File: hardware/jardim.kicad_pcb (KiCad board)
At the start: 2 copper layers, 100 x 100 mm, 67 parts, among them J1 DC_INPUT, J10 DHT22_AMB, J11 LIGHT_SENSOR_1, J12 LIGHT_SENSOR_2, J13 LEVEL_SENSOR_1, J14 LEVEL_SENSOR_2, J15 SOIL_HUMIDITY_SENSOR_1, J16 SOIL_HUMIDITY_SENSOR_2, J2 PUMP_1, J3 PUMP_2, J4 LIGHT_1, J5 LIGHT_2, J6 HEAT_2, J7 HEAT_2, J8 DS12B20_2, J9 DS18B20_1, Q1 IRLB8721, Q2 IRLB8721, Q3 IRLB8721, Q4 IRLB8721, Q5 IRLB8721, Q6 IRLB8721, U1 AM2302

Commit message: kicad otr
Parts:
- C1: value 100uF -> 220uF
- C5, C6, D3, Q2, R5, R6: moved to F.Cu
- R19, U1: moved to B.Cu
- moved J1 157.7 mm to (55.9, 45.8), turned to -90 degrees
- moved J2 121.7 mm to (55.9, 68.6), turned to -90 degrees
- moved J9 106.2 mm to (147.3, 83.7)
- moved J8 106.1 mm to (147.3, 71.1)
- moved J10 51.8 mm to (147.3, 96.4)
- moved J12 49.1 mm to (146.8, 125.7)
- moved J13 46.3 mm to (147.3, 134.6)
- moved J11 35.5 mm to (147.3, 111.7)
- moved J3 34.8 mm to (55.9, 81.3)
- moved J4 24.6 mm to (55.9, 94.0)
- moved J5 24.6 mm to (55.9, 106.7)
- moved J7 24.6 mm to (55.9, 132.1)
- moved J6 24.6 mm to (55.9, 119.4)
- moved R6 22.4 mm to (146.9, 45.7), turned to 180 degrees
- moved D3 20.8 mm to (125.3, 45.7)
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
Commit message: miniaturizando com grade menor
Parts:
- added SW1: SW_Push, Button_Switch_THT:SW_PUSH_6mm, F.Cu at (183.4, 118.4)
- added SW2: SW_Push, Button_Switch_THT:SW_PUSH_6mm, F.Cu at (183.4, 126.0)
- added SW3: SW_Push, Button_Switch_THT:SW_PUSH_6mm, F.Cu at (183.4, 133.6)
- added U2: DM-OLED096-636, oled:MODULE_DM-OLED096-636, F.Cu at (130.2, 125.1)
- R19, U1: moved to F.Cu
- moved R19 112.1 mm to (171.4, 65.4), turned to 180 degrees
- moved U1 82.8 mm to (148.0, 66.7), turned to 0 degrees
- moved J13 65.4 mm to (189.2, 84.4)
- moved J14 59.2 mm to (179.7, 84.6)
- moved R15 55.8 mm to (141.6, 99.1)
- moved J10 46.9 mm to (189.2, 75.5)
- moved D9 45.5 mm to (113.7, 127.6)
- moved D8 45.2 mm to (113.7, 116.2)
- moved D7 45.0 mm to (113.7, 104.8)
- moved D6 44.8 mm to (113.7, 93.3)
- moved R10 44.6 mm to (108.6, 109.9)
- moved R13 44.6 mm to (108.6, 112.4)
- moved R16 44.6 mm to (108.6, 125.1)
- moved R3 44.6 mm to (108.6, 71.8)
- moved R4 44.6 mm to (108.6, 84.5)
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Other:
- board text added: "220uF"
- board text added: "DC-DC 12V"
- board text added: "DC_IN_24V"
- board text added: "DHT22"
- board text added: "DOWN"
- board text added: "HEAT_1"
- board text added: "HEAT_2"
- board text added: "LIGHT_1"
- board text added: "LIGHT_2"
- board text added: "OK"
- board text added: "OLED 1306"
- board text added: "TEXTO"
- board text added: "UP"
- board text removed: "100uF"
- board text removed: "DC IN 24V"

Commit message: buzzer e textos
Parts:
- added BZ1: Buzzer, Buzzer_Beeper:Buzzer_12x9.5RM7.6, B.Cu at (161.9, 123.8)
- added D5: 1N5822, Diode_THT:D_DO-201AD_P15.24mm_Horizontal, B.Cu at (166.4, 133.3)
- added Q7: FQP30N06L, Package_TO_SOT_THT:TO-220-3_Horizontal_TabDown, B.Cu at (161.3, 105.1)
- added R20: 220, Resistor_THT:R_Axial_DIN0207_L6.3mm_D2.5mm_P10.16mm_Horizontal, B.Cu at (163.2, 111.1)
- added R21: 10k, Resistor_THT:R_Axial_DIN0207_L6.3mm_D2.5mm_P10.16mm_Horizontal, B.Cu at (163.2, 115.6)
- added SW4: SW_SPST, TerminalBlock_Phoenix:TerminalBlock_Phoenix_MKDS-1,5-2-5.08_1x02_P5.08mm_Horizontal, B.Cu at (100.8, 59.1)
- J6: value HEAT_2 -> HEAT_1
- Q1, Q2, Q3, Q4, Q5, Q6: value IRLB8721 -> FQP30N06L
- R19: footprint Resistor_THT:R_Axial_DIN0207_L6.3mm_D2.5mm_P10.16mm_Horizontal -> Resistor_THT:R_Axial_DIN0207_L6.3mm_D2.5mm_P7.62mm_Horizontal
- moved C1 68.1 mm to (163.8, 69.2)
- moved C2 67.5 mm to (168.9, 68.0)
- moved R13 7.75 mm to (114.9, 116.8)
- moved R3 7.75 mm to (114.9, 76.2)
- moved R4 7.75 mm to (114.9, 88.9)
- moved R10 7.75 mm to (114.9, 114.3)
- moved R16 7.75 mm to (114.9, 129.5)
- moved R7 7.75 mm to (114.9, 101.6)
- moved D4 5.85 mm to (109.9, 77.5)
- moved D7 5.85 mm to (109.9, 100.3)
- moved D9 5.85 mm to (109.9, 123.2)
- moved D2 5.85 mm to (109.9, 66.0)
- moved D6 5.85 mm to (109.9, 88.9)
- moved D8 5.85 mm to (109.9, 111.8)
- moved J2 3.17 mm to (100.8, 63.5)
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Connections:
- F1 pad 1: +24V -> Net-(SW4-B)
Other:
- board text added: "HEATER_1"
- board text added: "HEATER_2"
- board text added: "LEVEL_1"
- board text added: "LEVEL_2"
- board text added: "PUMP_1"
- board text added: "PUMP_2"
- board text added: "SOIL_H_1"
- board text added: "SOIL_H_2"
- board text added: "TEMP_1"
- board text added: "TEMP_2"
- board text added: "T_H_AMB"
- board text removed: "TEXTO"

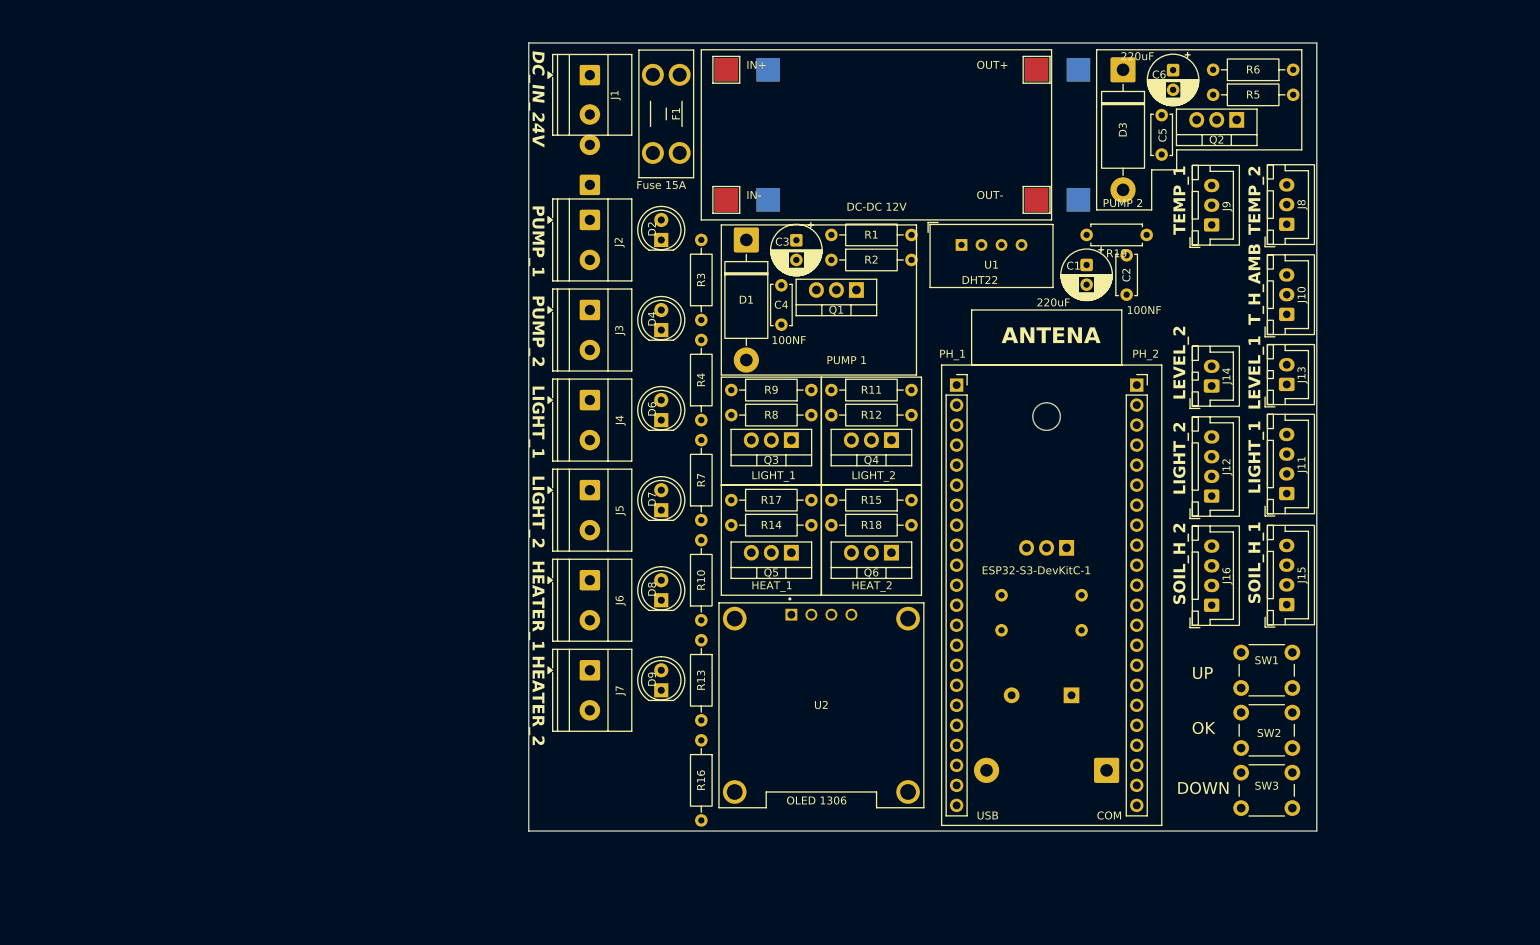
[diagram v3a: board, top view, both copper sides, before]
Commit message: avisos de serigrafia
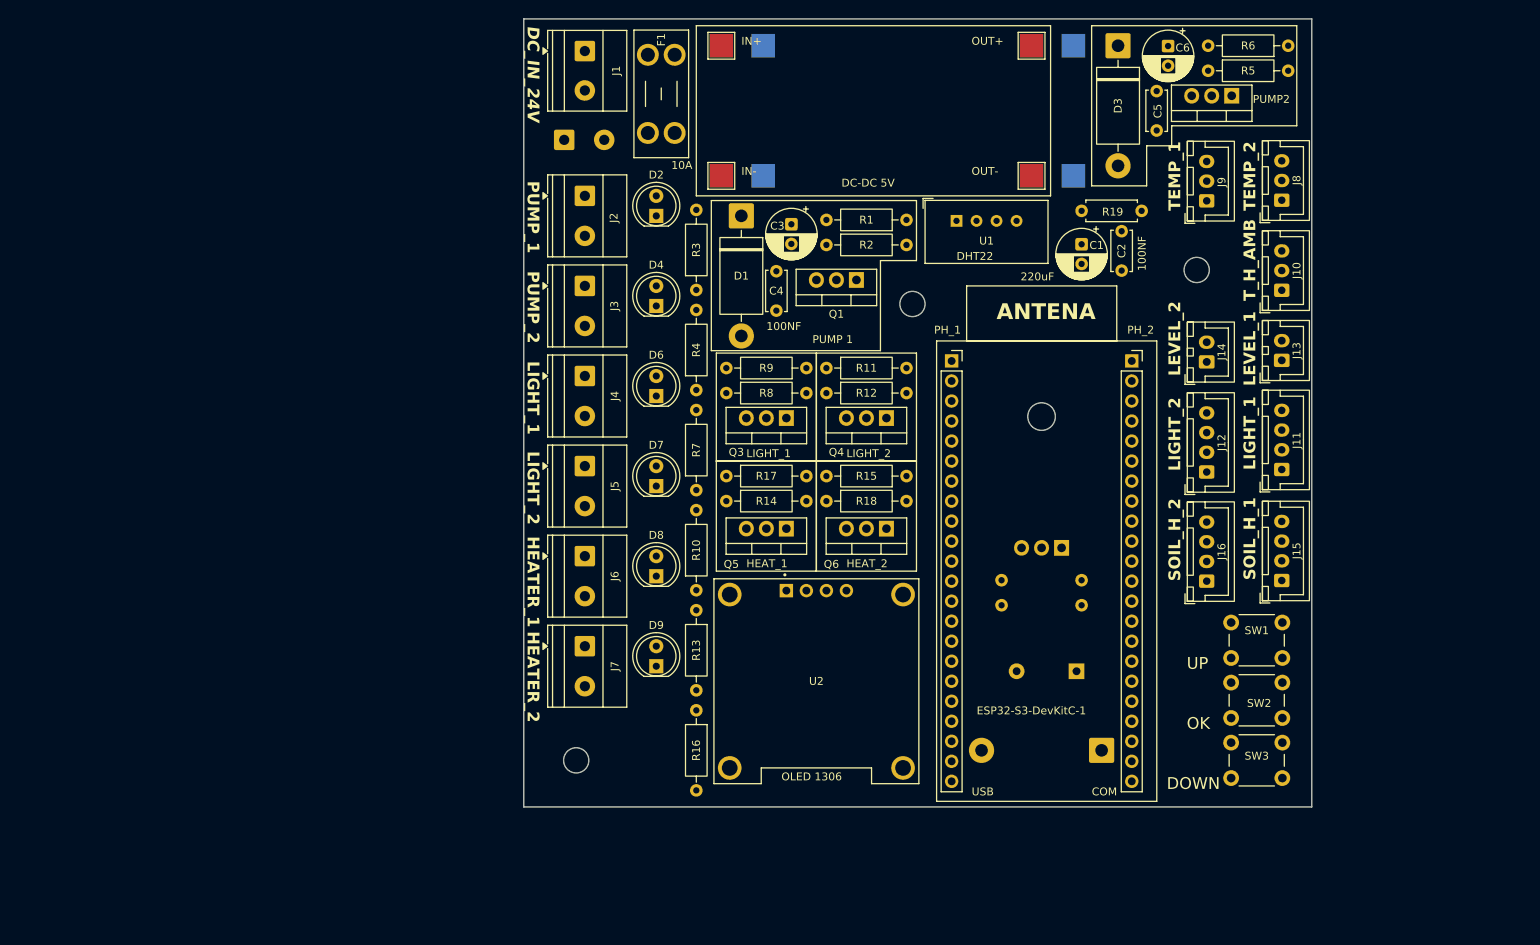
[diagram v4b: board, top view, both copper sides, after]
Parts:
- added H1: MountingHole_3.2mm_M3, MountingHole:MountingHole_3.2mm_M3, F.Cu at (177.8, 69.8)
- added h2: MountingHole_3.2mm_M3, MountingHole:MountingHole_3.2mm_M3, F.Cu at (141.7, 74.2)
- added h3: MountingHole_3.2mm_M3, MountingHole:MountingHole_3.2mm_M3, F.Cu at (99.1, 132.1)
- moved SW4 6.58 mm to (97.5, 53.3), turned to 0 degrees
- moved SW1 4.02 mm to (182.2, 114.6)
- moved SW2 4.02 mm to (182.2, 122.2)
- moved SW3 4.02 mm to (182.2, 129.8)
- moved R10 3.86 mm to (114.3, 110.5)
- moved R13 3.86 mm to (114.3, 113.0)
- moved R3 3.86 mm to (114.3, 72.4)
- moved R4 3.86 mm to (114.3, 85.1)
- moved R16 3.86 mm to (114.3, 125.7)
- moved R7 3.86 mm to (114.3, 97.8)
- moved R21 3.17 mm to (163.2, 112.4)
- moved BZ1 3.12 mm to (162.6, 120.8)
- moved J12 3.12 mm to (179.1, 95.5)
- moved J14 3.12 mm to (179.1, 81.5)
- moved J9 3.12 mm to (179.1, 61.1)
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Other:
- board text added: "10A"
- board text added: "10k"
- board text added: "DC-DC 5V"
- board text added: "PUMP2"
- board text removed: "DC-DC"
- board text removed: "Fuse 15A"
- board text removed: "PUMP 2"

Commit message: atribuindo gpio e furações com pad
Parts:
- removed H1: MountingHole_3.2mm_M3, MountingHole:MountingHole_3.2mm_M3
- added h1: MountingHole_3.2mm_M3_Pad_Via, MountingHole:MountingHole_3.2mm_M3_Pad_Via, F.Cu at (97.8, 132.7)
- h2, h3: value MountingHole_3.2mm_M3 -> MountingHole_3.2mm_M3_Pad_Via; footprint MountingHole:MountingHole_3.2mm_M3 -> MountingHole:MountingHole_3.2mm_M3_Pad_Via
- moved h3 100.4 mm to (177.8, 69.8)
- moved h2 0.72 mm to (142.2, 73.7)

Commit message: roteamento automatico
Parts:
- removed h1, h2, h3: MountingHole_3.2mm_M3_Pad_Via, MountingHole:MountingHole_3.2mm_M3_Pad_Via
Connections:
- J10 pad 2: unconnected-(J10-Pin_2-Pad2) -> /IO18
- J11 pad 2: unconnected-(J11-Pin_2-Pad2) -> /IO8
- J11 pad 3: unconnected-(J11-Pin_3-Pad3) -> /IO9
- J12 pad 2: unconnected-(J12-Pin_2-Pad2) -> /IO8
- J12 pad 3: unconnected-(J12-Pin_3-Pad3) -> /IO9
- J13 pad 1: unconnected-(J13-Pin_1-Pad1) -> /IO37
- J14 pad 1: unconnected-(J14-Pin_1-Pad1) -> /IO38
- J15 pad 2: unconnected-(J15-Pin_2-Pad2) -> /IO5
- J15 pad 3: unconnected-(J15-Pin_3-Pad3) -> /IO4
- J8 pad 2: unconnected-(J8-Pin_2-Pad2) -> /IO36
- J9 pad 2: unconnected-(J9-Pin_2-Pad2) -> /IO35
- R1 pad 1: /IO4 -> /IO10
- R12 pad 1: /IO7 -> /IO13
- R15 pad 1: /IO15 -> /IO14
- R18 pad 1: /IO16 -> /IO15
- R19 pad 2: /IO16 -> /IO17
- R20 pad 2: /IO17 -> /IO16
- R6 pad 1: /IO5 -> /IO11
- R9 pad 1: /IO6 -> /IO12
- SW1 pad 1: unconnected-(SW1-Pad1) -> /IO47
- SW1 pad 2: unconnected-(SW1-Pad2) -> GND
- SW2 pad 1: unconnected-(SW2-Pad1) -> /IO48
- SW2 pad 2: unconnected-(SW2-Pad2) -> GND
- SW3 pad 1: unconnected-(SW3-Pad1) -> /IO1
- SW3 pad 2: unconnected-(SW3-Pad2) -> GND
- U1 pad 2: /IO16 -> /IO17
- U2 pad 1: unconnected-(U2-GND-Pad1) -> GND
- U2 pad 2: unconnected-(U2-VCC_IN-Pad2) -> +5V
- U2 pad 3: unconnected-(U2-SCL-Pad3) -> /IO9
- U2 pad 4: unconnected-(U2-SDA-Pad4) -> /IO8
- U2 pad S1: (no net) -> unconnected-(U2-PadS1)
- U2 pad S2: (no net) -> unconnected-(U2-PadS2)
- U2 pad S3: (no net) -> unconnected-(U2-PadS3)
- U2 pad S4: (no net) -> unconnected-(U2-PadS4)
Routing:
- net GND: track 0.00 -> 459.2 mm, vias 0 -> 1
- net +12V: track 0.00 -> 253.8 mm
- net +5V: track 0.00 -> 251.4 mm, vias 0 -> 1
- net +24V: track 0.00 -> 192.5 mm, vias 0 -> 1
- net /IO11: track 0.00 -> 118.5 mm, vias 0 -> 1
- net Net-(D3-A): track 0.00 -> 95.0 mm
- net /IO9: track 0.00 -> 78.1 mm, vias 0 -> 1
- net /IO8: track 0.00 -> 63.5 mm
- net /IO36: track 0.00 -> 60.6 mm
- net /IO18: track 0.00 -> 59.9 mm
- net /IO35: track 0.00 -> 59.5 mm
- net /IO12: track 0.00 -> 58.8 mm
- net /IO10: track 0.00 -> 58.4 mm
- net /IO17: track 0.00 -> 57.0 mm
- net /IO1: track 0.00 -> 54.6 mm
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
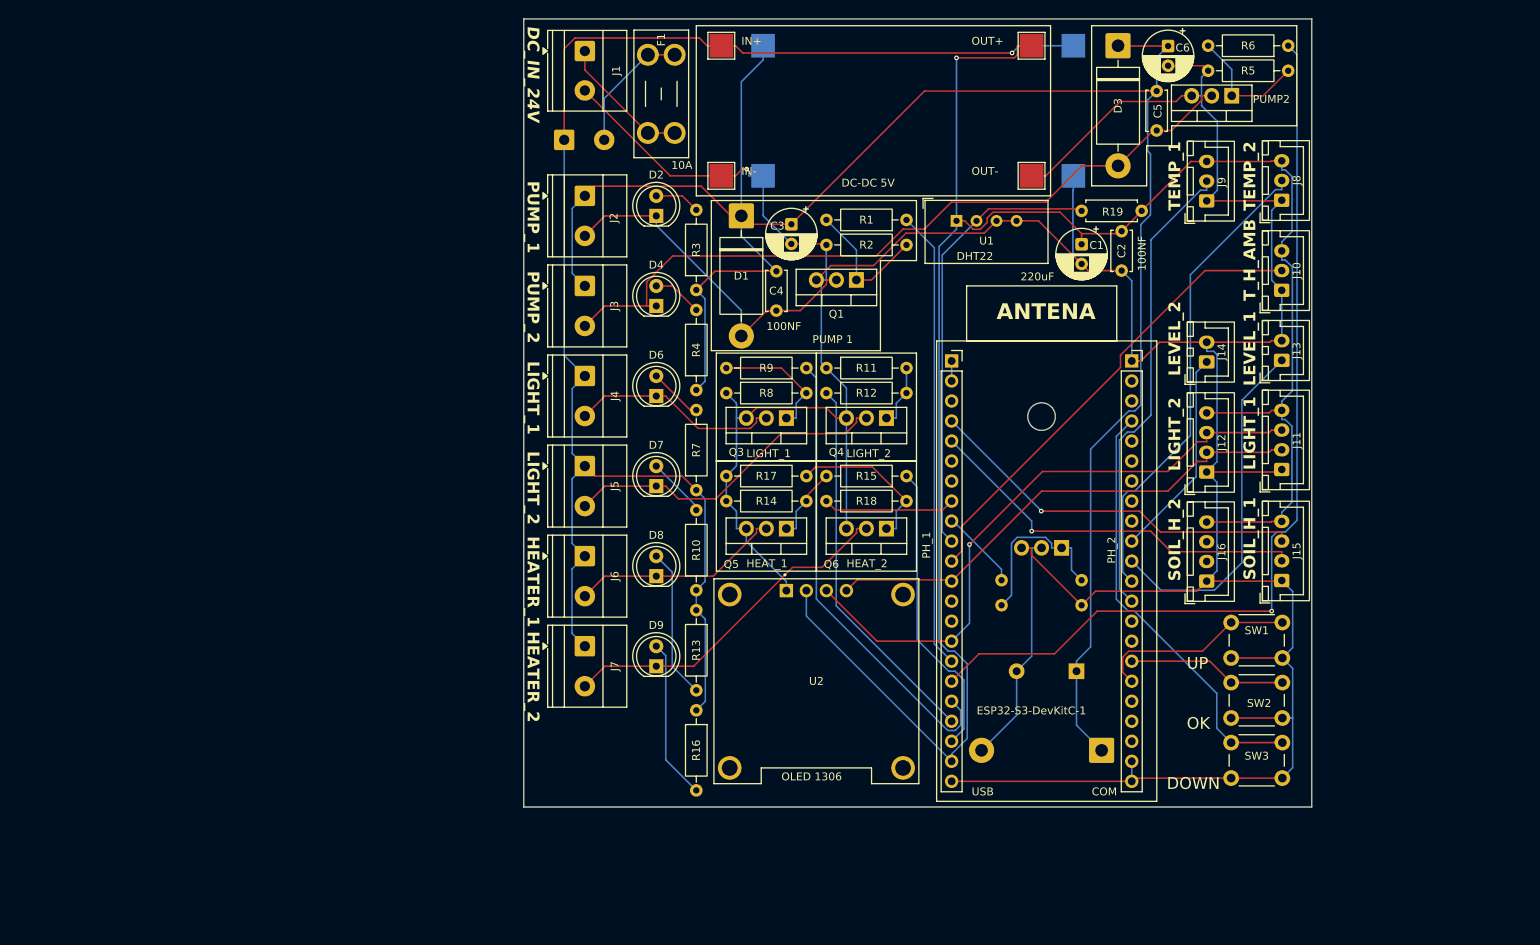
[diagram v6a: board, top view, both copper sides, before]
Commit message: adicionando os futos m3 novamente, rotemando com regras e classes 24v 12v e 5v
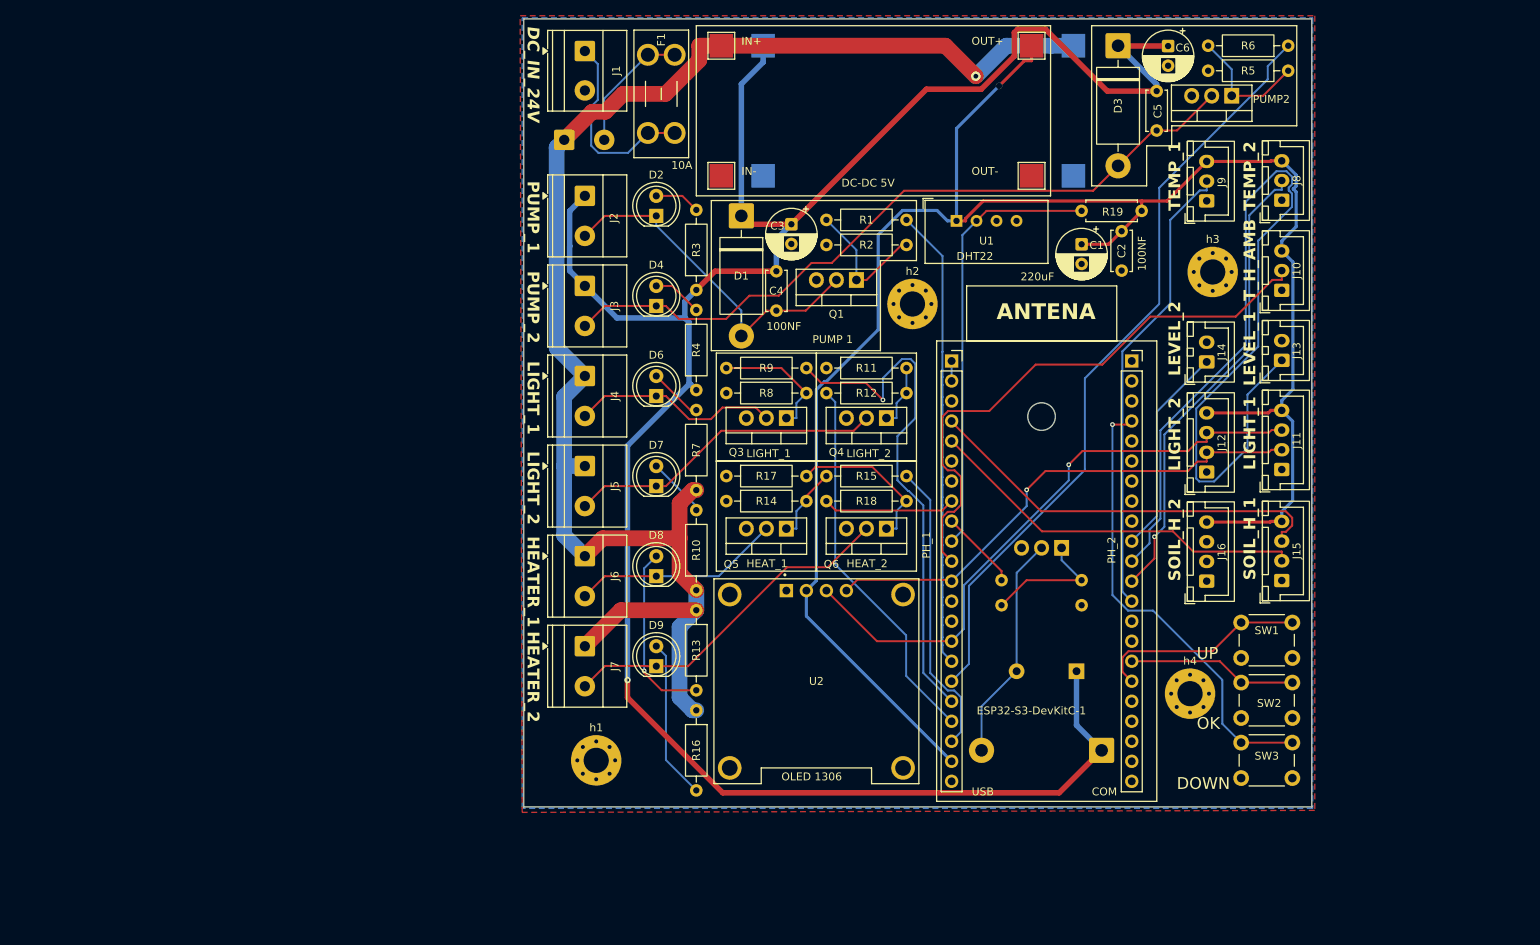
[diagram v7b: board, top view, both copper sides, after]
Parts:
- added h1: MountingHole_3.2mm_M3_Pad_Via, MountingHole:MountingHole_3.2mm_M3_Pad_Via, F.Cu at (101.6, 132.1)
- added h2: MountingHole_3.2mm_M3_Pad_Via, MountingHole:MountingHole_3.2mm_M3_Pad_Via, F.Cu at (141.7, 74.2)
- added h3: MountingHole_3.2mm_M3_Pad_Via, MountingHole:MountingHole_3.2mm_M3_Pad_Via, F.Cu at (179.8, 70.1)
- added h4: MountingHole_3.2mm_M3_Pad_Via, MountingHole:MountingHole_3.2mm_M3_Pad_Via, F.Cu at (177.0, 123.6)
- moved SW1 1.27 mm to (183.4, 114.6)
- moved SW2 1.27 mm to (183.4, 122.2)
- moved SW3 1.27 mm to (183.4, 129.8)
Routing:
- net GND: track 459.2 -> 0.00 mm, vias 1 -> 0
- net /IO37: track 44.7 -> 124.4 mm
- net +12V: track 253.8 -> 286.4 mm, vias 0 -> 1
- net /IO11: track 118.5 -> 98.3 mm, vias 1 -> 0
- net /IO18: track 59.9 -> 73.2 mm
- net +5V: track 251.4 -> 241.2 mm
- net Net-(J1-Pin_1): track 17.1 -> 25.1 mm
- net /IO12: track 58.8 -> 66.2 mm, vias 0 -> 1
- net Net-(Q7-G): track 21.8 -> 16.6 mm
- net Net-(D8-A): track 19.1 -> 23.0 mm, vias 0 -> 1
- net /IO1: track 54.6 -> 58.1 mm, vias 0 -> 1
- net /IO4: track 48.9 -> 52.2 mm, vias 1 -> 0
- net Net-(D3-A): track 95.0 -> 93.0 mm
- net +24V: track 192.5 -> 194.4 mm
- net Net-(D7-K): track 42.0 -> 40.4 mm
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- added copper zone on B.Cu, net GND
- added copper zone on F.Cu, net GND
